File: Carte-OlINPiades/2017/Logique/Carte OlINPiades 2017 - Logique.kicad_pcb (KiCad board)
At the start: 2 copper layers, 100 x 100 mm, 92 parts, among them P1 CONN_01X32, P2 CONN_01X32, P3 CONN_01X02, P4 CONN_01X06, P5 CONN_01X02, P6 CONN_01X02, P7 CONN_FREE_01X03, Q1 MMPQ2907A, Q2 MMPQ2907A, Q3 MMPQ2907A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

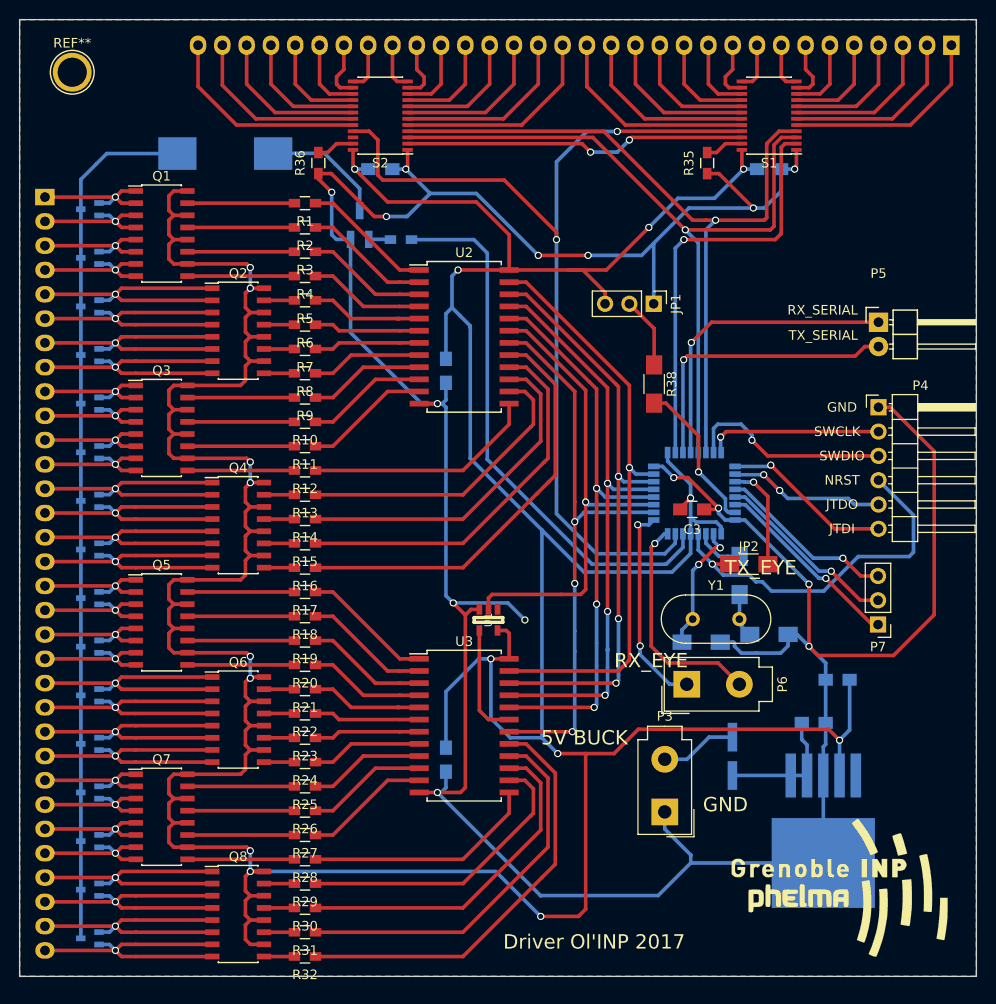
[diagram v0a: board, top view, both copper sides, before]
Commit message: ajout 3.3V pour esp
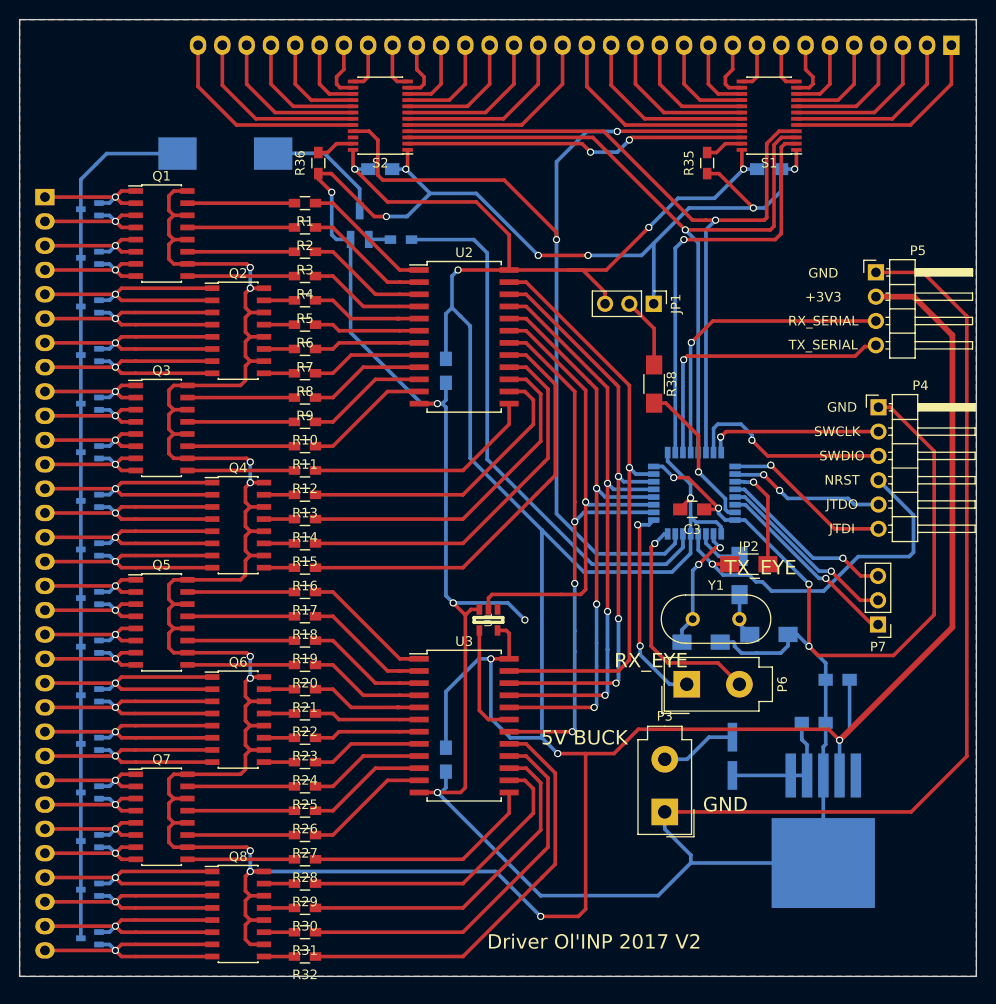
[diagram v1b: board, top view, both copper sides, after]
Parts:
- removed G***: LOGO, drawings:phelma_logo
- removed REF**: 1pin, Connect:1pin
- P5: value CONN_01X02 -> CONN_01X04; footprint Pin_Headers:Pin_Header_Angled_1x02 -> Pin_Headers:Pin_Header_Angled_1x04_Pitch2.54mm
- moved P5 5.22 mm to (191.5, 82.4)
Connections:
- P5 pad 1: RX_SERIAL -> GND
- P5 pad 2: TX_SERIAL -> +3V3
- S2 pad 22: Net-(S2-Pad22) -> (no net)
- U1 pad 1: Net-(U1-Pad1) -> (no net)
- U5 pad 5: Net-(U5-Pad5) -> (no net)
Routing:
- net GND: track 334.8 -> 426.2 mm
- net +3V3: track 470.2 -> 527.1 mm
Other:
- board text added: "+3V3"
- board text added: "Driver Ol'INP 2017 V2"
- board text removed: "Driver Ol'INP 2017"
